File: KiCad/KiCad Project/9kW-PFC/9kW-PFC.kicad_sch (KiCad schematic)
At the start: 0 parts

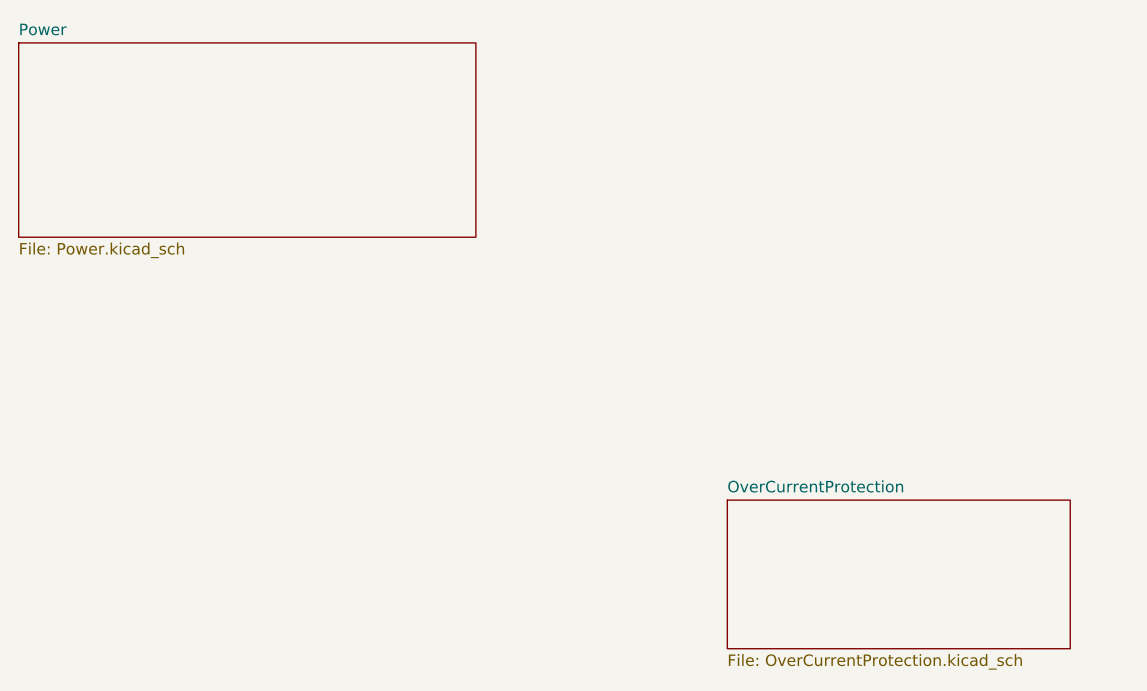
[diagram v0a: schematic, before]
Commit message: Started on Over Current Protection
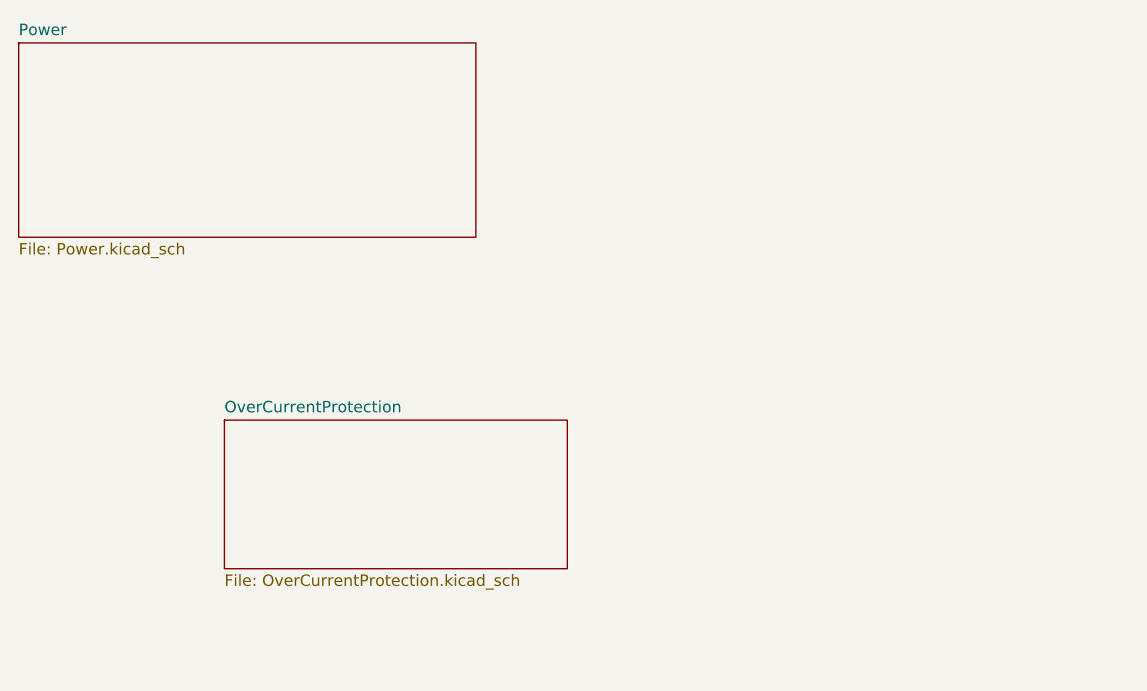
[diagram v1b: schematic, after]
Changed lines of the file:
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@@
 	)
 	(sheet
-		(at 93.98 77.47)
+		(at 38.1 68.58)
 		(size 38.1 16.51)
 		(fields_autoplaced yes)
@@
 		)
 		(property "Sheetname" "OverCurrentProtection"
-			(at 93.98 76.7584 0)
+			(at 38.1 67.8684 0)
 			(effects
 				(font
@@
 		)
 		(property "Sheetfile" "OverCurrentProtection.kicad_sch"
-			(at 93.98 94.5646 0)
+			(at 38.1 85.6746 0)
 			(effects
 				(font
